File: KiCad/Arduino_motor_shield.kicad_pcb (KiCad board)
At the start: 2 copper layers, 25.9 x 59.9 mm, 16 parts, among them J1 Conn_01x15, J2 Barrel_Jack_Switch, J3 Conn_01x15, J4 Screw_Terminal_01x05, U1 TB6612FNG

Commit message: Small fixes to alignment
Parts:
- J1: value Conn_01x15 -> Arduino header 1
- J2: value Barrel_Jack_Switch -> DC jack
- J3: value Conn_01x15 -> Arduino header 2
- J4: value Screw_Terminal_01x05 -> Motors conn
- JP1: value SolderJumper_3_Open -> Solder jumper
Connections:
- J1 pad 13: /~{RESET2} -> /~{RESET}
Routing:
- net /~{RESET}: track 0.00 -> 28.0 mm
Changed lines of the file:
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@@
   (net 63 "/AO2")
   (net 64 "/AO1")
-  (net 65 "/~{RESET2}")
   (footprint "Capacitor_SMD:CP_Elec_6.3x5.8" (layer "F.Cu")
     (at 126.36276 119.634 -90)
@@
         (effects (font (size 1 1) (thickness 0.15)))
     )
-    (fp_text value "SolderJumper_3_Open" (at 0 2 90) (layer "F.Fab")
+    (fp_text value "Solder jumper" (at 0 2 90) (layer "F.Fab")
         (effects (font (size 1 1) (thickness 0.15)))
     )
@@
         (effects (font (size 1 1) (thickness 0.15)) (justify mirror))
     )
-    (fp_text value "Conn_01x15" (at 0 -38.33) (layer "B.Fab")
+    (fp_text value "Arduino header 1" (at 0 -38.33) (layer "B.Fab")
         (effects (font (size 1 1) (thickness 0.15)) (justify mirror))
     )
@@
       (net 4 "+5V") (pinfunction "Pin_12") (pintype "passive"))
     (pad "13" thru_hole oval (at 0 -30.48) (size 1.7 1.7) (drill 1) (layers "*.Cu" "*.Mask")
-      (net 65 "/~{RESET2}") (pinfunction "Pin_13") (pintype "passive"))
+      (net 40 "/~{RESET}") (pinfunction "Pin_13") (pintype "passive"))
     (pad "14" thru_hole oval (at 0 -33.02) (size 1.7 1.7) (drill 1) (layers "*.Cu" "*.Mask")
       (net 7 "GND") (pinfunction "Pin_14") (pintype "passive"))
@@
         (effects (font (size 1 1) (thickness 0.15)) (justify mirror))
     )
-    (fp_text value "Screw_Terminal_01x05" (at 10 -5.66) (layer "B.Fab")
+    (fp_text value "Motors conn" (at 10 -5.66) (layer "B.Fab")
         (effects (font (size 1 1) (thickness 0.15)) (justify mirror))
     )
@@
         (effects (font (size 1 1) (thickness 0.15)) (justify mirror))
     )
-    (fp_text value "Conn_01x15" (at 0 -38.33) (layer "B.Fab")
+    (fp_text value "Arduino header 2" (at 0 -38.33) (layer "B.Fab")
         (effects (font (size 1 1) (thickness 0.15)) (justify mirror))
     )
@@
         (effects (font (size 1 1) (thickness 0.15)) (justify mirror))
     )
-    (fp_text value "Barrel_Jack_Switch" (at -6.2 5.5) (layer "B.Fab")
+    (fp_text value "DC jack" (at -6.2 5.5) (layer "B.Fab")
         (effects (font (size 1 1) (thickness 0.15)) (justify mirror))
     )
@@
     (effects (font (size 0.5 0.5) (thickness 0.125) bold) (justify right bottom))
   )
-  (gr_text "TU-Sofia" (at 145.542 113.284 90) (layer "F.Cu")
+  (gr_text "TU-Sofia" (at 145.542 113.03 90) (layer "F.Cu")
     (effects (font (size 1 1) (thickness 0.15)) (justify left bottom))
   )
-  (gr_text "Iliyan Antov" (at 145.542 99.568 90) (layer "F.Cu")
+  (gr_text "Iliyan Antov" (at 145.288 99.06 90) (layer "F.Cu")
     (effects (font (size 1 1) (thickness 0.15)) (justify left bottom))
   )
-  (gr_text "2024" (at 145.542 83.312 90) (layer "F.Cu")
+  (gr_text "2024" (at 145.542 83.058 90) (layer "F.Cu")
     (effects (font (size 1 1) (thickness 0.15)) (justify left bottom))
   )
@@
   (segment (start 131.48276 109.3) (end 131.48276 105.704) (width 0.75) (layer "F.Cu") (net 38))
   (segment (start 132.30076 110.118) (end 131.48276 109.3) (width 0.75) (layer "F.Cu") (net 38))
+  (segment (start 123.952 80.43324) (end 123.952 76.708) (width 0.25) (layer "B.Cu") (net 40))
+  (segment (start 124.714 75.946) (end 134.70476 75.946) (width 0.25) (layer "B.Cu") (net 40))
+  (segment (start 123.952 76.708) (end 124.714 75.946) (width 0.25) (layer "B.Cu") (net 40))
+  (segment (start 134.70476 75.946) (end 141.60276 82.844) (width 0.25) (layer "B.Cu") (net 40))
+  (segment (start 126.36276 82.844) (end 123.952 80.43324) (width 0.25) (layer "B.Cu") (net 40))
   (segment (start 137.18393 80.18) (end 132.386365 80.18) (width 0.25) (layer "F.Cu") (net 42))
   (segment (start 141.60276 90.464) (end 139.91 88.77124) (width 0.25) (layer "F.Cu") (net 42))

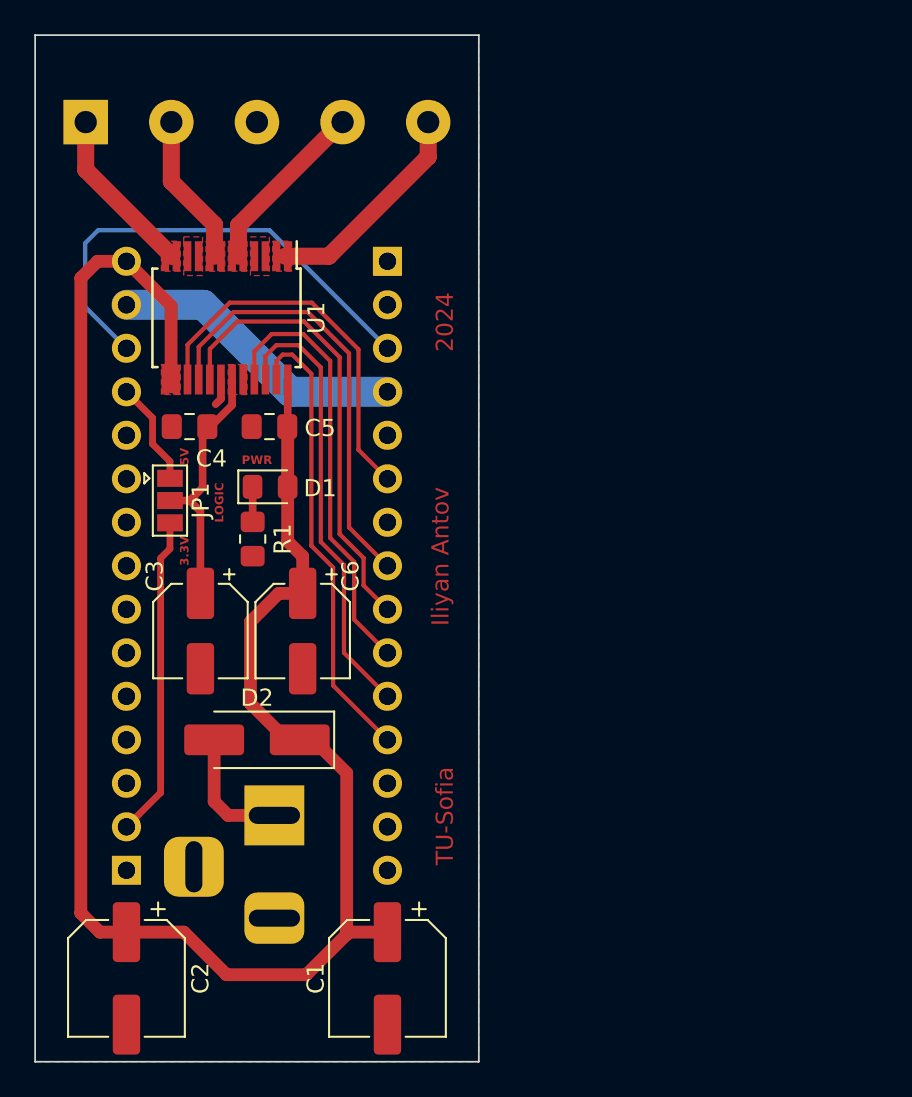
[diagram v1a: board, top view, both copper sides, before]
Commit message: Added mounting holes
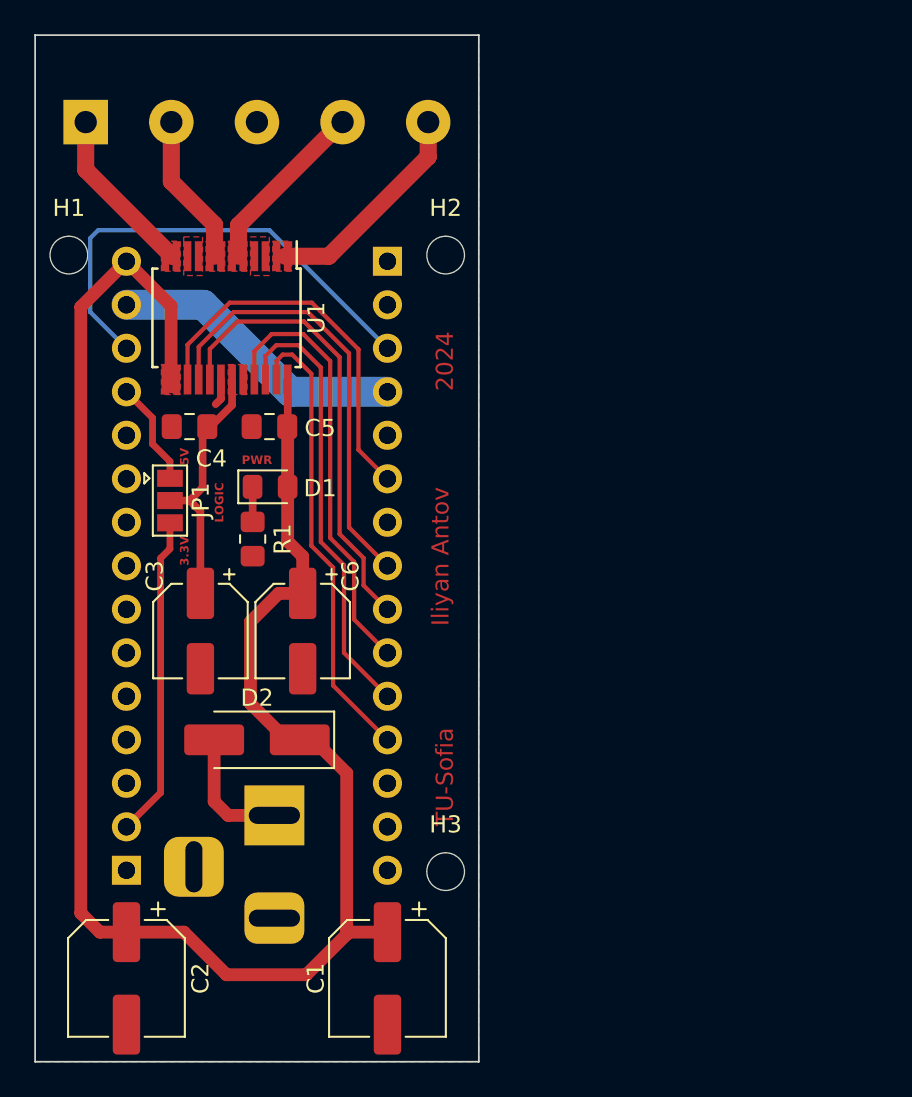
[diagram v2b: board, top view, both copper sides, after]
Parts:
- added H1: MountingHole, MountingHole:MountingHole_2.2mm_M2_ISO7380, F.Cu at (123.0, 77.4)
- added H2: MountingHole, MountingHole:MountingHole_2.2mm_M2_ISO7380, F.Cu at (145.0, 77.4)
- added H3: MountingHole, MountingHole:MountingHole_2.2mm_M2_ISO7380, F.Cu at (145.0, 113.4)
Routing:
- net +12V: track 107.1 -> 106.1 mm
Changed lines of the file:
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@@
   (net 63 "/AO2")
   (net 64 "/AO1")
+  (footprint "MountingHole:MountingHole_2.2mm_M2_ISO7380" (layer "F.Cu")
+    (at 145 113.4)
+    (descr "Mounting Hole 2.2mm, no annular, M2, ISO7380")
+    (tags "mounting hole 2.2mm no annular m2 iso7380")
+    (property "Sheetfile" "Arduino_motor_shield.kicad_sch")
+    (property "Sheetname" "")
+    (property "ki_description" "Mounting Hole without connection")
+    (property "ki_keywords" "mounting hole")
+    (attr exclude_from_pos_files)
+    (fp_text reference "H3" (at 0 -2.75) (layer "F.SilkS")
+        (effects (font (size 1 1) (thickness 0.15)))
+    )
+    (fp_text value "MountingHole" (at 0 2.75) (layer "F.Fab")
+        (effects (font (size 1 1) (thickness 0.15)))
+    )
+    (fp_text user "${REFERENCE}" (at 0 0) (layer "F.Fab")
+        (effects (font (size 1 1) (thickness 0.15)))
+    )
+    (fp_circle (center 0 0) (end 1.75 0)
+      (stroke (width 0.15) (type solid)) (fill none) (layer "Cmts.User"))
+    (fp_circle (center 0 0) (end 2 0)
+      (stroke (width 0.05) (type solid)) (fill none) (layer "F.CrtYd"))
+    (pad "" np_thru_hole circle (at 0 0) (size 2.2 2.2) (drill 2.2) (layers "*.Cu" "*.Mask"))
+  )
   (footprint "Capacitor_SMD:CP_Elec_6.3x5.8" (layer "F.Cu")
     (at 126.36276 119.634 -90)
@@
     )
   )
+  (footprint "MountingHole:MountingHole_2.2mm_M2_ISO7380" (layer "F.Cu")
+    (at 123 77.4)
+    (descr "Mounting Hole 2.2mm, no annular, M2, ISO7380")
+    (tags "mounting hole 2.2mm no annular m2 iso7380")
+    (property "Sheetfile" "Arduino_motor_shield.kicad_sch")
+    (property "Sheetname" "")
+    (property "ki_description" "Mounting Hole without connection")
+    (property "ki_keywords" "mounting hole")
+    (attr exclude_from_pos_files)
+    (fp_text reference "H1" (at 0 -2.75) (layer "F.SilkS")
+        (effects (font (size 1 1) (thickness 0.15)))
+    )
+    (fp_text value "MountingHole" (at 0 2.75) (layer "F.Fab")
+        (effects (font (size 1 1) (thickness 0.15)))
+    )
+    (fp_text user "${REFERENCE}" (at 0 0) (layer "F.Fab")
+        (effects (font (size 1 1) (thickness 0.15)))
+    )
+    (fp_circle (center 0 0) (end 1.75 0)
+      (stroke (width 0.15) (type solid)) (fill none) (layer "Cmts.User"))
+    (fp_circle (center 0 0) (end 2 0)
+      (stroke (width 0.05) (type solid)) (fill none) (layer "F.CrtYd"))
+    (pad "" np_thru_hole circle (at 0 0) (size 2.2 2.2) (drill 2.2) (layers "*.Cu" "*.Mask"))
+  )
   (footprint "Capacitor_SMD:CP_Elec_5x5.4" (layer "F.Cu")
     (at 130.68076 99.354 -90)
@@
       (rotate (xyz 0 0 0))
     )
+  )
+  (footprint "MountingHole:MountingHole_2.2mm_M2_ISO7380" (layer "F.Cu")
+    (at 145 77.4)
+    (descr "Mounting Hole 2.2mm, no annular, M2, ISO7380")
+    (tags "mounting hole 2.2mm no annular m2 iso7380")
+    (property "Sheetfile" "Arduino_motor_shield.kicad_sch")
+    (property "Sheetname" "")
+    (property "ki_description" "Mounting Hole without connection")
+    (property "ki_keywords" "mounting hole")
+    (attr exclude_from_pos_files)
+    (fp_text reference "H2" (at 0 -2.75) (layer "F.SilkS")
+        (effects (font (size 1 1) (thickness 0.15)))
+    )
+    (fp_text value "MountingHole" (at 0 2.75) (layer "F.Fab")
+        (effects (font (size 1 1) (thickness 0.15)))
+    )
+    (fp_text user "${REFERENCE}" (at 0 0) (layer "F.Fab")
+        (effects (font (size 1 1) (thickness 0.15)))
+    )
+    (fp_circle (center 0 0) (end 1.75 0)
+      (stroke (width 0.15) (type solid)) (fill none) (layer "Cmts.User"))
+    (fp_circle (center 0 0) (end 2 0)
+      (stroke (width 0.05) (type solid)) (fill none) (layer "F.CrtYd"))
+    (pad "" np_thru_hole circle (at 0 0) (size 2.2 2.2) (drill 2.2) (layers "*.Cu" "*.Mask"))
   )
   (footprint "Connector_PinSocket_2.54mm:PinSocket_1x15_P2.54mm_Vertical" (layer "B.Cu")
@@
     (effects (font (size 0.5 0.5) (thickness 0.125) bold) (justify right bottom))
   )
-  (gr_text "TU-Sofia" (at 145.542 113.03 90) (layer "F.Cu")
+  (gr_text "TU-Sofia" (at 145.542 110.744 90) (layer "F.Cu")
     (effects (font (size 1 1) (thickness 0.15)) (justify left bottom))
   )
@@
     (effects (font (size 1 1) (thickness 0.15)) (justify left bottom))
   )
-  (gr_text "2024" (at 145.542 83.058 90) (layer "F.Cu")
+  (gr_text "2024" (at 145.542 85.344 90) (layer "F.Cu")
     (effects (font (size 1 1) (thickness 0.15)) (justify left bottom))
   )
@@
   (segment (start 133.604 103.58962) (end 135.71838 105.704) (width 0.75) (layer "F.Cu") (net 3))
   (segment (start 132.20476 119.42) (end 136.866 119.42) (width 0.75) (layer "F.Cu") (net 3))
+  (segment (start 126.36276 77.764) (end 123.698 80.42876) (width 0.75) (layer "F.Cu") (net 3))
   (segment (start 136.48276 105.704) (end 137.28476 105.704) (width 0.75) (layer "F.Cu") (net 3))
   (segment (start 139.22276 116.72) (end 139.43676 116.934) (width 0.75) (layer "F.Cu") (net 3))
-  (segment (start 123.698 78.74) (end 123.698 115.824) (width 0.75) (layer "F.Cu") (net 3))
-  (segment (start 124.808 116.934) (end 126.36276 116.934) (width 0.75) (layer "F.Cu") (net 3))
+  (segment (start 123.698 115.824) (end 124.808 116.934) (width 0.75) (layer "F.Cu") (net 3))
   (segment (start 133.604 98.806) (end 133.604 103.58962) (width 0.75) (layer "F.Cu") (net 3))
   (segment (start 135.77976 84.666) (end 135.77976 87.38624) (width 0.45) (layer "F.Cu") (net 3))
+  (segment (start 124.808 116.934) (end 126.36276 116.934) (width 0.75) (layer "F.Cu") (net 3))
   (segment (start 139.22276 107.642) (end 139.22276 116.72) (width 0.75) (layer "F.Cu") (net 3))
   (segment (start 136.652 97.154) (end 135.256 97.154) (width 0.75) (layer "F.Cu") (net 3))
@@
   (segment (start 139.43676 116.934) (end 141.60276 116.934) (width 0.75) (layer "F.Cu") (net 3))
   (segment (start 135.71838 105.704) (end 136.48276 105.704) (width 0.75) (layer "F.Cu") (net 3))
-  (segment (start 124.674 77.764) (end 123.698 78.74) (width 0.75) (layer "F.Cu") (net 3))
   (segment (start 136.866 119.42) (end 139.22276 117.06324) (width 0.75) (layer "F.Cu") (net 3))
-  (segment (start 123.698 115.824) (end 124.808 116.934) (width 0.75) (layer "F.Cu") (net 3))
   (segment (start 135.256 97.154) (end 133.604 98.806) (width 0.75) (layer "F.Cu") (net 3))
   (segment (start 139.22276 117.06324) (end 139.22276 116.72) (width 0.75) (layer "F.Cu") (net 3))
@@
   (segment (start 137.28476 105.704) (end 139.22276 107.642) (width 0.75) (layer "F.Cu") (net 3))
   (segment (start 126.36276 77.764) (end 128.969686 80.370926) (width 0.75) (layer "F.Cu") (net 3))
-  (segment (start 126.36276 77.764) (end 124.674 77.764) (width 0.75) (layer "F.Cu") (net 3))
   (segment (start 126.36276 116.934) (end 129.71876 116.934) (width 0.75) (layer "F.Cu") (net 3))
+  (segment (start 123.698 80.42876) (end 123.698 115.824) (width 0.75) (layer "F.Cu") (net 3))
   (segment (start 127.88676 88.432) (end 127.88676 86.908) (width 0.4) (layer "F.Cu") (net 4))
   (segment (start 127.88676 86.908) (end 126.36276 85.384) (width 0.4) (layer "F.Cu") (net 4))
@@
   (segment (start 131.48276 109.3) (end 131.48276 105.704) (width 0.75) (layer "F.Cu") (net 38))
   (segment (start 132.30076 110.118) (end 131.48276 109.3) (width 0.75) (layer "F.Cu") (net 38))
-  (segment (start 123.952 80.43324) (end 123.952 76.708) (width 0.25) (layer "B.Cu") (net 40))
+  (segment (start 134.70476 75.946) (end 141.60276 82.844) (width 0.25) (layer "B.Cu") (net 40))
+  (segment (start 126.36276 82.844) (end 124.25 80.73124) (width 0.25) (layer "B.Cu") (net 40))
   (segment (start 124.714 75.946) (end 134.70476 75.946) (width 0.25) (layer "B.Cu") (net 40))
-  (segment (start 123.952 76.708) (end 124.714 75.946) (width 0.25) (layer "B.Cu") (net 40))
-  (segment (start 134.70476 75.946) (end 141.60276 82.844) (width 0.25) (layer "B.Cu") (net 40))
-  (segment (start 126.36276 82.844) (end 123.952 80.43324) (width 0.25) (layer "B.Cu") (net 40))
+  (segment (start 124.25 76.41) (end 124.714 75.946) (width 0.25) (layer "B.Cu") (net 40))
+  (segment (start 124.25 80.73124) (end 124.25 76.41) (width 0.25) (layer "B.Cu") (net 40))
   (segment (start 137.18393 80.18) (end 132.386365 80.18) (width 0.25) (layer "F.Cu") (net 42))
   (segment (start 141.60276 90.464) (end 139.91 88.77124) (width 0.25) (layer "F.Cu") (net 42))
@@
       )
     )
+  )
+  (zone (net 0) (net_name "") (layer "F.Mask") (hatch edge 0.5)
+    (connect_pads (clearance 0.25))
+    (min_thickness 0.25) (filled_areas_thickness no)
+    (fill yes (thermal_gap 0.5) (thermal_bridge_width 0.5))
+    (polygon
+      (pts
+        (xy 121 64.5)
+        (xy 147 64.5)
+        (xy 147 124.5)
+        (xy 121 124.5)
+      )
+    )
